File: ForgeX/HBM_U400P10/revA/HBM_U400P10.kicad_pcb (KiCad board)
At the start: 2 copper layers, 32.2 x 69.6 mm, 36 parts, among them J1 Conn_02x05_Odd_Even, J2 Screw_Terminal_01x03, Q1 STF24N60M2, Q2 STF24N60M2, U1 INA199xxDCK, U2 EG2104S, U3 SN74LVC1G32DBVR, U7 AMS1117-3.3

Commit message: add bootstrap resistor on HBM mdoule
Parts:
- added R6: 5, Resistor_SMD:R_1206_3216Metric_Pad1.30x1.75mm_HandSolder, F.Cu at (167.6, 105.0)
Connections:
- D1 pad 1: +12V -> Net-(D1-A)
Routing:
- net Net-(D1-A): track 0.00 -> 3.81 mm
- net +12V: track 42.8 -> 39.4 mm
- net GND: vias 79 -> 76

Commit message: hbm_U40010 sot-363 package updates
, better handsoldering
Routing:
- net /GATE_{H}: track 18.2 -> 17.0 mm
- net Net-(D1-A): track 3.81 -> 3.00 mm
- net /VBOOT: track 6.22 -> 5.61 mm

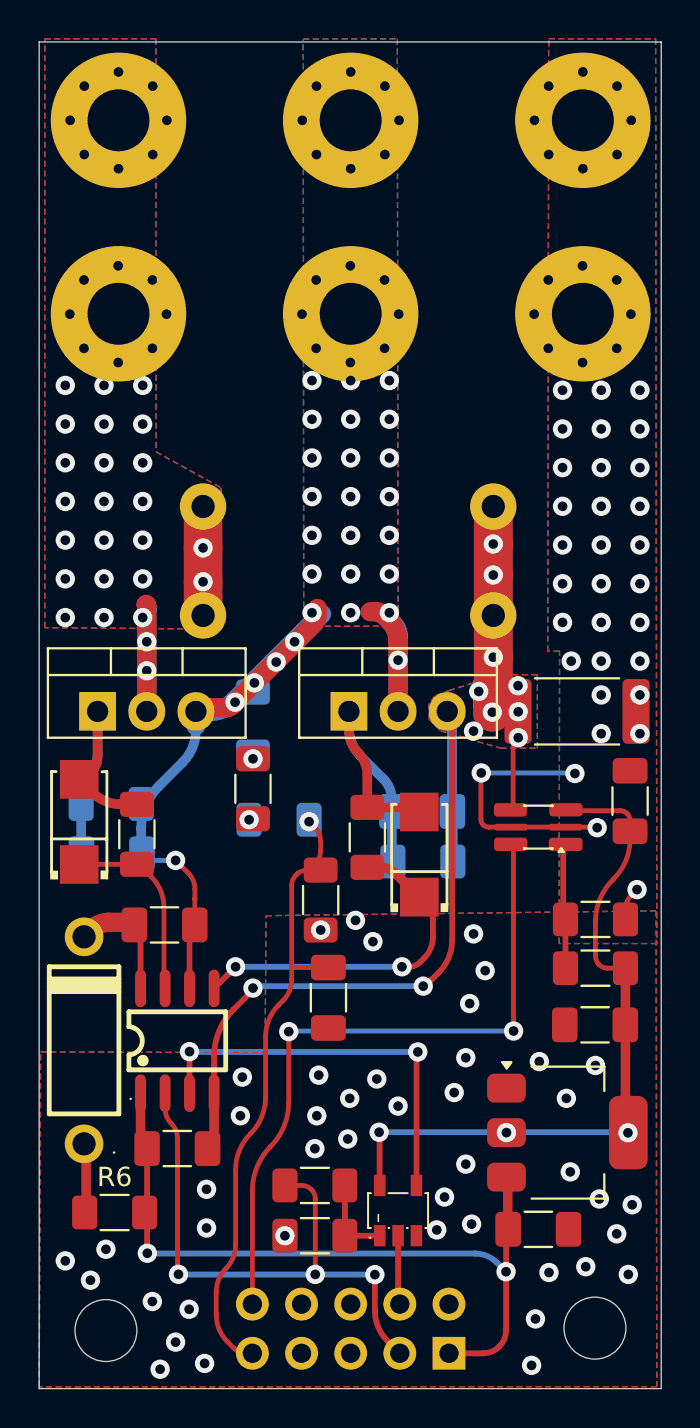
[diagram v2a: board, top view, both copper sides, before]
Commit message: Major redesign & Reworks
* Star grounding scheme enforced across the whole ForgeX design....
* Viper26 based PSU designed
* Better signal integrity & decoupling on LVP and major reroute
* Laminated DC bus (Biplanar) , instead of (Coplanar) , for heavily reduced bus inductance & equivelant Electrolytics ESL
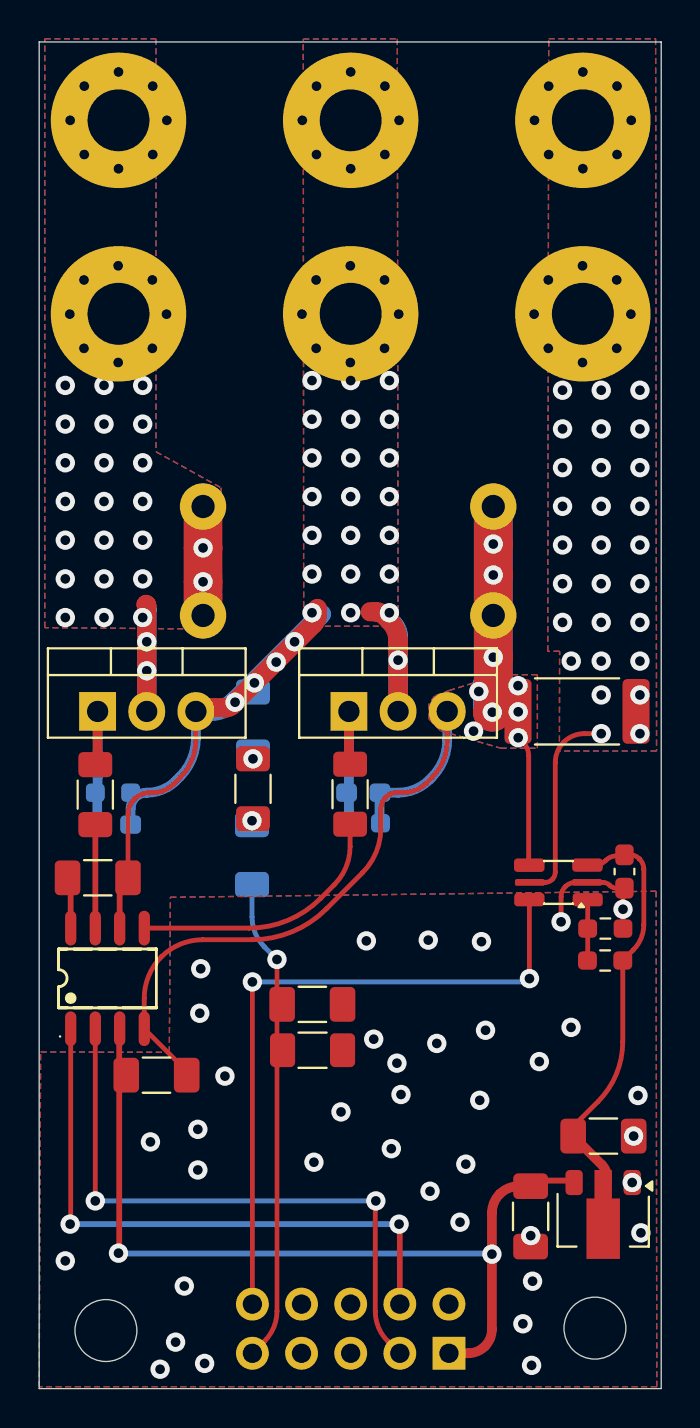
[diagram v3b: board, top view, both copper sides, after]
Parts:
- removed D1: BYV26EGP-E3/73, EasyEDA:DO-15_BD3.1-L6.7-P10.70-D0.9-FD
- removed D2, D3: SS34_C8678, EasyEDA:SMA_L4.3-W2.6-LS5.2-RD
- removed JP1, JP2: Jumper_2_Open, Resistor_SMD:R_1206_3216Metric_Pad1.30x1.75mm_HandSolder
- removed R6: 5, Resistor_SMD:R_1206_3216Metric_Pad1.30x1.75mm_HandSolder
- removed U3: SN74LVC1G32DBVR, EasyEDA:SOT-23-5_L3.0-W1.7-P0.95-LS2.8-BR
- C2, C3: value 2.2n -> 1n; footprint Capacitor_SMD:C_1206_3216Metric_Pad1.33x1.80mm_HandSolder -> Capacitor_SMD:C_0603_1608Metric_Pad1.08x0.95mm_HandSolder
- C4: footprint Capacitor_SMD:C_1206_3216Metric_Pad1.33x1.80mm_HandSolder -> Capacitor_SMD:C_0603_1608Metric_Pad1.08x0.95mm_HandSolder
- R1: value 2.5m -> 5m
- R11, R12: value 22 -> 10
- R2, R3, R4, R5: footprint Resistor_SMD:R_1206_3216Metric_Pad1.30x1.75mm_HandSolder -> Resistor_SMD:R_0603_1608Metric_Pad0.98x0.95mm_HandSolder
- U2: value EG2104S -> L6385ED; footprint EasyEDA:SOIC-8_L5.0-W4.0-P1.27-LS6.0-BL -> EasyEDA:SOIC-8_L4.9-W3.9-P1.27-LS6.0-BL
- U7: footprint Package_TO_SOT_SMD:SOT-223-3_TabPin2 -> Package_TO_SOT_SMD:SOT-89-3
- moved R26 7.77 mm to (177.8, 96.6), turned to 0 degrees
- moved C38 5.77 mm to (192.9, 101.1), turned to 0 degrees
- moved U7 4.89 mm to (192.9, 105.4), turned to -90 degrees
- moved U2 4.84 mm to (167.2, 92.9)
- moved C8 4.22 mm to (166.7, 87.7)
- moved C7 3.94 mm to (169.8, 97.9)
- moved R5 3.68 mm to (180.4, 84.9)
- moved C4 3.65 mm to (194.0, 87.4), turned to -90 degrees
- moved C2 3.19 mm to (180.5, 83.3)
- moved U1 3.04 mm to (190.5, 87.9)
- moved R11 2.97 mm to (166.6, 83.4)
- moved R12 2.40 mm to (179.8, 83.4)
- moved R27 2.28 mm to (174.7, 86.5), turned to 90 degrees
- moved C3 1.51 mm to (167.6, 85.0)
- moved C9 0.90 mm to (177.8, 94.2), turned to 0 degrees
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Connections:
- net /GATE_{H} renamed Net-(Q2-G)
- net /PHASE_{150} renamed Net-(R27-Pad2)
- net /PHASE_{300} renamed Net-(R28-Pad2)
- net /VBOOT renamed Net-(U2-VBOOT)
- net MGD_GND renamed /Shunt+
- J2 pad 3: GND -> GNDPWR
- R1 pad 2: GND -> GNDPWR
- U1 pad 5: GND -> GNDPWR
- U2 pad 1: +12V -> LIN
- U2 pad 3: Net-(U2-#SD) -> +12V
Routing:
- net LIN: track 3.56 -> 31.3 mm, vias 0 -> 2
- net Net-(U2-#SD): track 20.6 -> 0.00 mm, vias 2 -> 0
- net +3.3V: track 36.6 -> 21.6 mm, vias 3 -> 0
- net GNDPWR: track 0.00 -> 10.8 mm, vias 0 -> 28
- net Net-(Q2-G): track 17.0 -> 8.24 mm
- net Net-(Q1-G): track 17.0 -> 8.77 mm
- net GND: track 15.2 -> 7.18 mm, vias 76 -> 38
- net Phase_Cnd: track 32.6 -> 25.3 mm
- net +12V: track 39.4 -> 45.5 mm
- net /HS_GateSig: track 10.0 -> 5.35 mm
- net /LS_GateSig: track 18.3 -> 13.8 mm, vias 2 -> 0
- net Net-(JP1-A): track 4.40 -> 0.00 mm
- net Phase: track 44.2 -> 48.3 mm, vias 27 -> 26
- net Net-(U1-REF): track 6.46 -> 3.15 mm
- net Net-(D1-A): track 3.00 -> 0.00 mm
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- added copper zone on B.Cu, net GNDPWR
- added copper zone on F.Cu, net GNDPWR

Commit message: HBM quick change
Swapped L6385ED MGD to L6388ED, since it is a better fit for the application
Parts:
- removed U2: L6385ED, EasyEDA:SOIC-8_L4.9-W3.9-P1.27-LS6.0-BL
- added U3: L6388ED, EasyEDA:SO-8_L4.9-W3.9-P1.27-LS5.9-BL, F.Cu at (167.2, 92.9)
